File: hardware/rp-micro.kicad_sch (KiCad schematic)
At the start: 45 parts, among them J1 USB_C_Receptacle_USB2.0, J2 Conn_01x12, J3 Conn_01x12, J4 Conn_01x05, SW1 BOOT, SW2 RESET, U1 RT9013-33GB, U2 W25Q16JVUXIQ, U3 RP2040, Y1 12MHz

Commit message: Update track
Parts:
- renumbered C3 to C1, C17 to C10, C8 to C11, C9 to C12, C10 to C13, C11 to C14, C12 to C15, C13 to C16, C14 to C17, C1 to C2, C2 to C3, C15 to C8, C16 to C9, R11 to R10, R12 to R11, R9 to R12, R3 to R2, R4 to R3, R5 to R4, R2 to R5, R10 to R9
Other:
- note added: "Board"
- note added: "Flash"
- note added: "Power"
- note added: "RP2040"
- note added: "USB"
- moved on the sheet: C1, C10, C11, C12, C13, C14, C15, C16, C17, C2, C3, C4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

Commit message: Update
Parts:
- removed C1, C4: 2.2uF, Capacitor_SMD:C_0402_1005Metric, symbol Device:C
- removed R1: 200, Resistor_SMD:R_0402_1005Metric, symbol Device:R
- removed R10, R9: 4.7k, Resistor_SMD:R_0402_1005Metric, symbol Device:R
- removed R6: 27, Resistor_SMD:R_0402_1005Metric, symbol Device:R
- added C15: 0.1uF, Capacitor_SMD:C_0402_1005Metric, symbol Device:C
- added R5: 27, Resistor_SMD:R_0402_1005Metric, symbol Device:R
- added TP2, TP3: TestPoint, TestPoint:TestPoint_Pad_D1.0mm, symbol Connector:TestPoint
- C1: renamed from C2; MFR. Part # CL05A105KA5NQNC -> CL05A105KA5NQNC
- C16: renamed from C17; value 2.2uF -> 1uF; JLCPCB Part # C12530 -> C52923; MFR. Part # CL05A225MQ5NSNC -> CL05A105KA5NQNC; Note (none) -> ${REFERENCE} close to pin 45 (VREG_OUT)
- C2: renamed from C3; MFR. Part # CL05A105KA5NQNC -> CL05A105KA5NQNC
- C4: renamed from C6; value 15pF -> 20pF; JLCPCB Part # C1548 -> C1554; MFR. Part # 0402CG150J500NT -> 0402CG200J500NT
- C5: renamed from C7; value 15pF -> 20pF; JLCPCB Part # C1548 -> C1554; MFR. Part # 0402CG150J500NT -> 0402CG200J500NT
- C8: renamed from C10; value 2.2uF -> 1uF; JLCPCB Part # C12530 -> C52923; MFR. Part # CL05A225MQ5NSNC -> CL05A105KA5NQNC; Note (none) -> ${REFERENCE} close to pin 44 (VREG_IN)
- J2, J3, J4: now left out of the parts list
- LD1: JLCPCB Part # C434419 -> C2286; MFR. Part # SZYY0603R -> KT-0603R
- Y1: footprint Crystal:Crystal_SMD_2520-4Pin_2.5x2.0mm -> Crystal:Crystal_SMD_3225-4Pin_3.2x2.5mm; JLCPCB Part # C2149204 -> C9002; MFR. Part # 2TJ412000HYGBC -> X322512MSB4SI
- renumbered C12 to C10, C13 to C11, C14 to C12, C15 to C13, C16 to C14, C5 to C3, C8 to C6, C9 to C7, C11 to C9, R2 to R1, R13 to R10, R3 to R2, R5 to R3, R7 to R6, R8 to R7, R11 to R8, R12 to R9
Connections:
- net +3V3: now also U3.43 (ADC_AVDD), C15.1
- net GND: now also J1.S1 (SHIELD), C15.2; no longer J4.3 (Pin_3)
- net SWCLK: now also TP3.1; no longer J4.1 (Pin_1)
- net SWDIO: now also TP2.1; no longer J4.2 (Pin_2)
- net USB_D+: now also J1.A6 (D+), J1.B6 (D+), R4.1; no longer U3.46 (USB_DM)
- net USB_D-: now also J1.A7 (D-), J1.B7 (D-), R5.1; no longer R4.2, U3.47 (USB_DP)
- net 10: now reaches U3.13 (GPIO10)
- net 10: now also J4.1 (Pin_1)
- net 11: now reaches U3.14 (GPIO11)
- net 11: now also J4.2 (Pin_2)
- net 12: now reaches U3.15 (GPIO12)
- net 12: now also J4.3 (Pin_3)
- net 16_SDA renamed 16
- net 17_SCL renamed 17
- new net: R5.2, U3.46 (USB_DM)
- new net: R4.2, U3.47 (USB_DP)
- no-connect marks 12 -> 8
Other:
- moved on the sheet: C16, C3, TP1

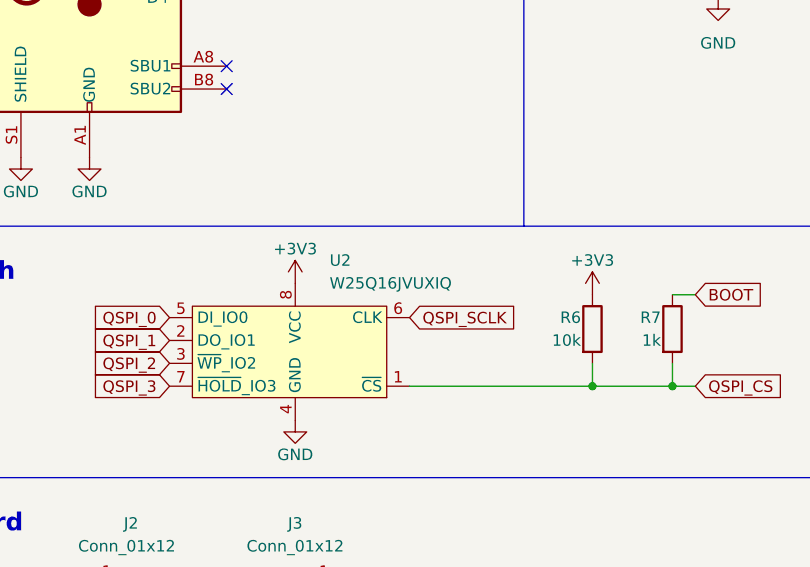
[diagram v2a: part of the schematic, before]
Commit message: Replace flash to W25Q64JVXGIQ
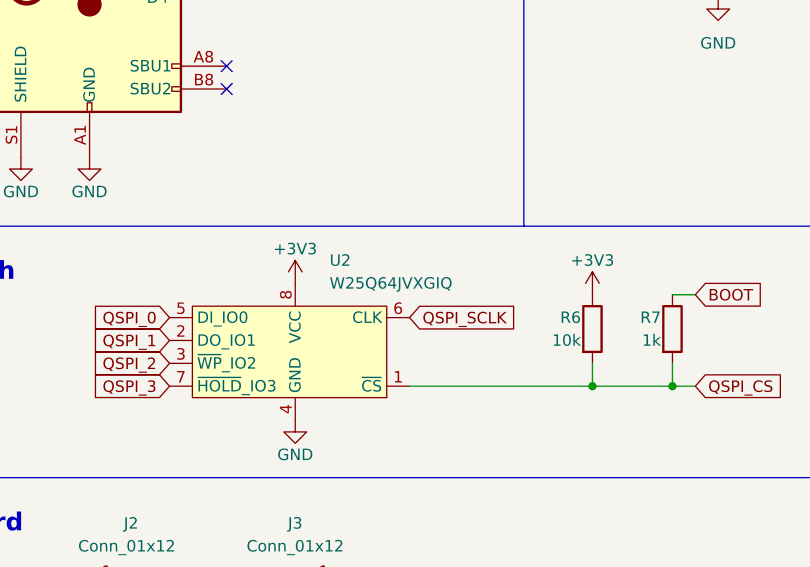
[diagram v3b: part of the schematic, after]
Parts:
- U2: value W25Q16JVUXIQ -> W25Q64JVXGIQ; footprint rp-micro:USON-8 (2x3mm) -> rp-micro:XSON-8 (4x4mm); JLCPCB Part # C2843335 -> C2940195; MFR. Part # W25Q16JVUXIQ -> W25Q64JVXGIQ
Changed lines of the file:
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@@
       (effects (font (size 1.27 1.27)) (justify left))
     )
-    (property "Value" "W25Q16JVUXIQ" (id 1) (at 185.42 82.55 0)
+    (property "Value" "W25Q64JVXGIQ" (id 1) (at 185.42 82.55 0)
       (effects (font (size 1.27 1.27)) (justify left))
     )
-    (property "Footprint" "rp-micro:USON-8 (2x3mm)" (id 2) (at 172.72 96.52 0)
+    (property "Footprint" "rp-micro:XSON-8 (4x4mm)" (id 2) (at 172.72 96.52 0)
       (effects (font (size 1.27 1.27)) hide)
     )
@@
       (effects (font (size 1.27 1.27)) hide)
     )
-    (property "MFR. Part #" "W25Q16JVUXIQ" (id 5) (at 181.61 90.17 0)
-      (effects (font (size 1.27 1.27)) hide)
-    )
-    (property "JLCPCB Part #" "C2843335" (id 4) (at 181.61 90.17 0)
+    (property "MFR. Part #" "W25Q64JVXGIQ" (id 5) (at 181.61 90.17 0)
+      (effects (font (size 1.27 1.27)) hide)
+    )
+    (property "JLCPCB Part #" "C2940195" (id 4) (at 181.61 90.17 0)
       (effects (font (size 1.27 1.27)) hide)
     )
@@
     )
     (path "/d2001dae-fd82-477a-8cad-63341df48a63"
-      (reference "U2") (unit 1) (value "W25Q16JVUXIQ") (footprint "rp-micro:USON-8 (2x3mm)")
+      (reference "U2") (unit 1) (value "W25Q64JVXGIQ") (footprint "rp-micro:XSON-8 (4x4mm)")
     )
     (path "/50ad4bf2-ea72-452c-bfb7-e3a68f1faf14"

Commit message: Improve 3v3 route
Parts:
- C16: Note ${REFERENCE} close to pin 45 (VREG_OUT) -> ${REFERENCE} close to pin 44 (VREG_IN)
- C8: Note ${REFERENCE} close to pin 44 (VREG_IN) -> ${REFERENCE} close to pin 45 (VREG_OUT)
- TP2: value TestPoint -> SWDIO
- TP3: value TestPoint -> SWCLK
- U2: symbol rp-micro:W25Q16JVUXIQ -> rp-micro:W25Q64JVXGIQ
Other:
- moved on the sheet: C10, C11, C12, C13, C14, C15, C16, C3, C4, C5, C6, C7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

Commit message: Update note
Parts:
- C8: Note ${REFERENCE} close to pin 45 (VREG_OUT) -> ${REFERENCE} close to pin 45 (VREG_VOUT)
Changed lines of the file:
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@@
       (effects (font (size 1.27 1.27)) hide)
     )
-    (property "Note" "${REFERENCE} close to pin 45 (VREG_OUT)" (id 6) (at 74.93 153.67 0))
+    (property "Note" "${REFERENCE} close to pin 45 (VREG_VOUT)" (id 6) (at 74.93 153.67 0))
     (pin "1")
     (pin "2")
